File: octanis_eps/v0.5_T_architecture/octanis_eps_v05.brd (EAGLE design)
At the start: 80 x 50 mm, 141 parts, among them IC1 OPA2333DGK, Q1 32.768kHz, Q100 BSS123, U1 CSD16327Q3_DQG_8, U10 CSD16327Q3_DQG_8, U11 CSD16327Q3_DQG_8, U12 TPS630250YFFT, U2 CSD16327Q3_DQG_8, U3 CSD16327Q3_DQG_8, U4 MSP430G2544, U5 TPS2022D, U6 TPS630250YFFT, U7 TPS630250YFFT, U8 TPS61232, U9 BQ24650_RVA_16

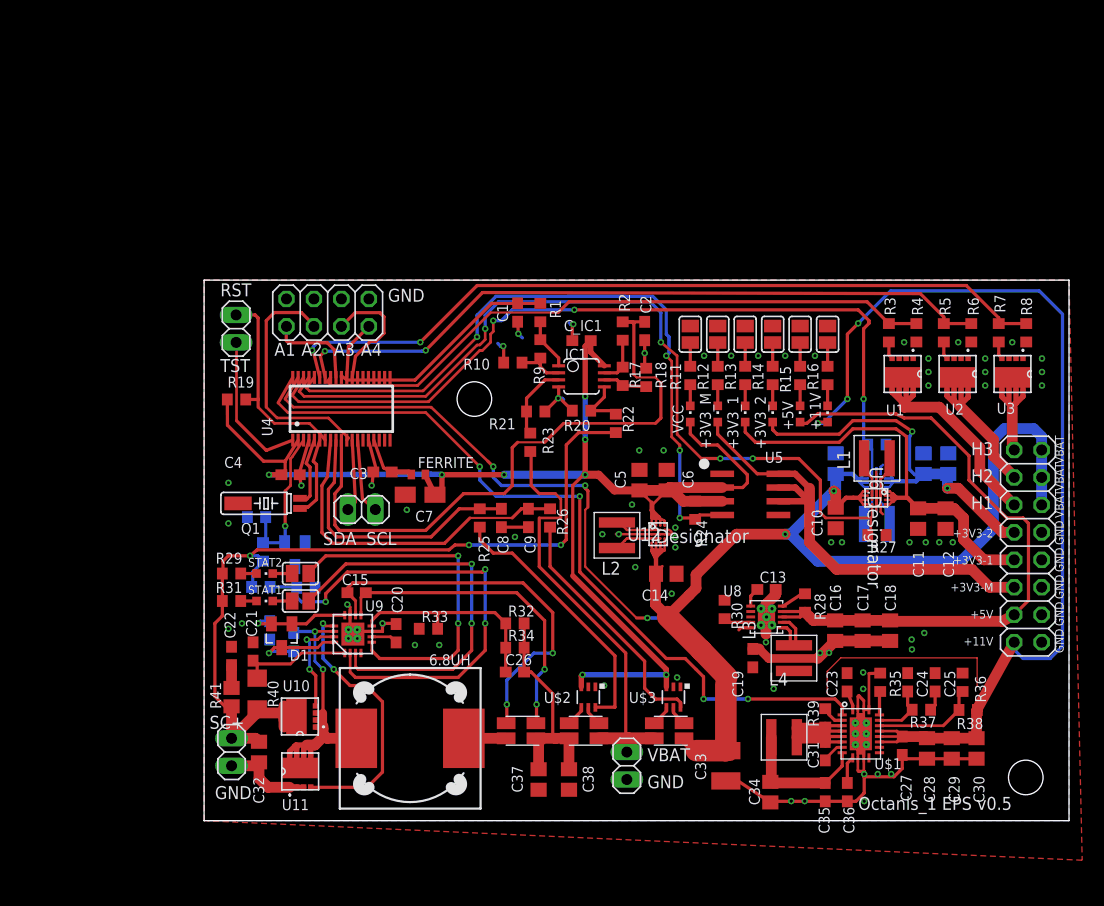
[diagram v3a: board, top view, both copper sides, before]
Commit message: replaced MSP430 for more efficient model. added mosfet circuit braker to schematic
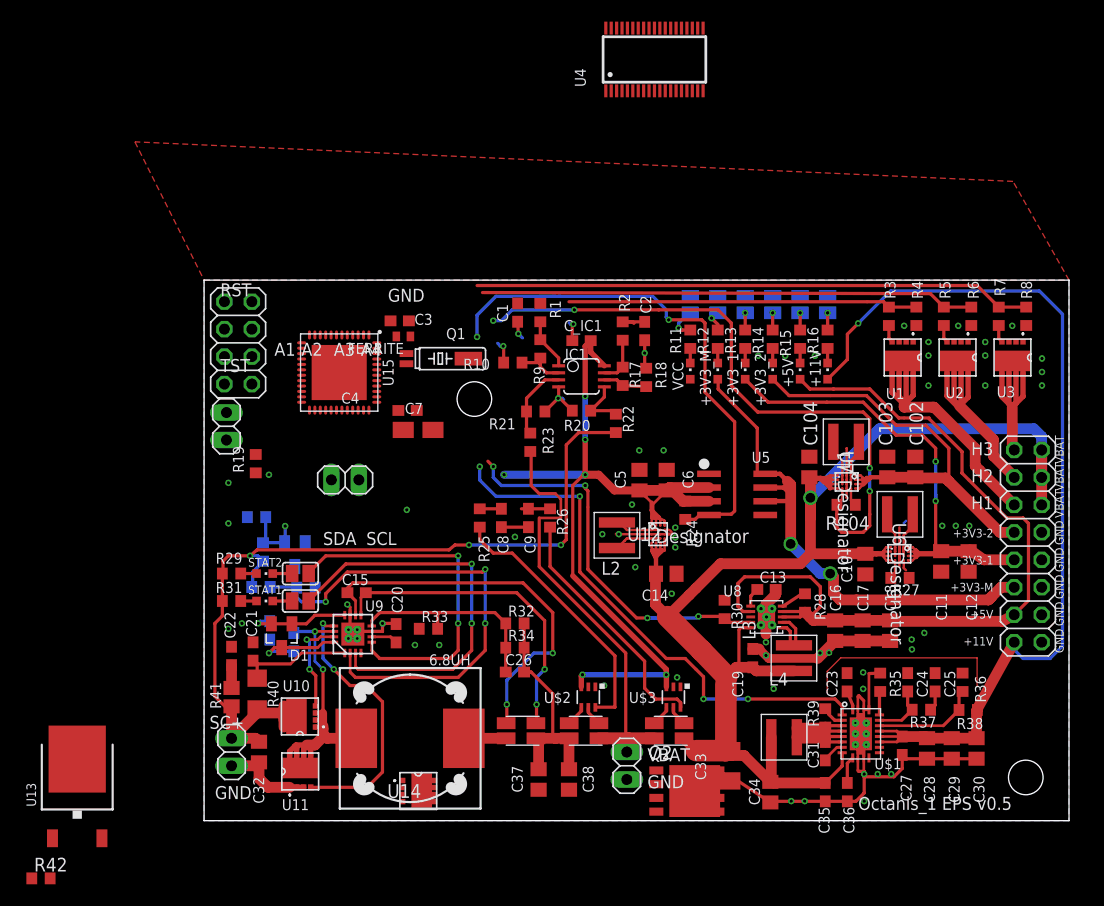
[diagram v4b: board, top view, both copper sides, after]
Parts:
- added Q2: BSC340N08NS3G, transistor-power:PG-TDSON-8
- added R42: dnp, resistor:R0603
- added U13: (no value), Seeed-OPL-ic:TO-252
- added U14: CSD16327Q3_DQG_8, texasinstruments:DQG8
- added U15: MSP430FR5969, chips:S-PVQFN-N48
- R35: value 270k -> 100k
- moved U4 43.4 mm to (41.7, 70.4)
- moved Q1 23.0 mm to (23.1, 42.7), turned to 270 degrees
- moved C3 14.1 mm to (18.1, 46.2), turned to 0 degrees
- moved FERRITE 12.8 mm to (18.4, 44.8), turned to 0 degrees
- moved C4 12.3 mm to (18.8, 37.9)
- moved JP2 9.07 mm to (2.07, 36.5), turned to 90 degrees
- moved JP1 8.74 mm to (3.15, 44.2), turned to 90 degrees
- moved L100 8.12 mm to (59.4, 35.0), flipped to the top, turned to 0 degrees
- moved R104 6.26 mm to (59.4, 29.2), flipped to the top, turned to 0 degrees
- moved R19 6.20 mm to (4.78, 33.0), turned to 270 degrees
- moved C7 6.00 mm to (19.8, 36.1), turned to 180 degrees
- moved L1 5.60 mm to (64.4, 28.3)
- moved U6 5.60 mm to (64.3, 24.7)
- moved C10 5.07 mm to (61.2, 23.7)
- moved R27 4.50 mm to (64.4, 22.5)
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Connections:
- removed net N$30: Q1.P1, U4.6
- removed net N$36: Q1.P2, U4.5
- removed net N$75: JP2.2, U4.1
- removed net N$93: JP2.1, R19.1, U4.7
- removed net N$99: C3.1, FERRITE.2, U4.16
- new net AGND: C3.2, U15.41, U15.44, U15.47
- new net N$10: C3.1, FERRITE.1, U15.48
- new net N$13: JP2.1, R19.1, U15.23
- new net N$15: JP2.2, U15.22
- new net N$16: Q1.P1, U15.46
- new net N$17: Q1.P2, U15.45
- new net N$9: R42.1, U$1.P$13
- net +3V3: now also FERRITE.2, U15.37; no longer FERRITE.1, U4.2
- net A_EXT1: now also JP1.7, U15.16; no longer JP1.1, U4.30
- net A_EXT2: now also JP1.5, U15.17; no longer JP1.3, U4.11
- net A_EXT3: now also JP1.3, U15.18; no longer JP1.5, U4.27
- net A_EXT4: now also JP1.1, U15.19; no longer JP1.7, U4.28
- net EN_12V: now also U15.28; no longer U4.38
- net EN_3V3_1: now also U15.34; no longer U4.35
- net EN_3V3_2: now also U15.35; no longer U4.36
- net EN_3V3_M: now also U15.33; no longer U4.34
- net EN_5V: now also U15.29; no longer U4.37
- net EN_SC: now also U15.27; no longer U4.3
- net GND: now also R42.2, U15.36, U15.VSS_QFN; no longer C3.2, U4.15, U4.4
- net I2C_SCL: now also U15.32; no longer U4.13
- net I2C_SDA: now also U15.31; no longer U4.12
- net I_IN: now also U15.2; no longer U4.9
- net I_OUT: now also U15.1; no longer U4.8
- net V_BAT: now also U15.9; no longer U4.29
- net V_SC: now also U15.3; no longer U4.10
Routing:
- net EN_3V3_1: track 78.4 -> 1.80 mm, vias 4 -> 0
- net V_SC: track 58.7 -> 3.12 mm
- net +3V3: track 140.0 -> 86.3 mm, vias 8 -> 7
- net I_OUT: track 31.5 -> 2.65 mm
- net EN_HEAT1: track 59.2 -> 32.3 mm
- net EN_12V: track 73.3 -> 49.5 mm
- net I_IN: track 25.8 -> 2.00 mm
- net A_EXT2: track 22.4 -> 0.00 mm
- net V_BAT: track 21.6 -> 0.00 mm
- net EN_HEAT3: track 73.0 -> 51.6 mm, vias 2 -> 0
- net EN_HEAT2: track 66.2 -> 45.7 mm, vias 2 -> 0
- net N$93: track 19.1 -> 0.00 mm
- net EN_5V: track 53.7 -> 37.6 mm, vias 3 -> 4
- net +5V: track 60.3 -> 76.1 mm
- net EN_3V3_M: track 64.1 -> 48.6 mm, vias 4 -> 2
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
